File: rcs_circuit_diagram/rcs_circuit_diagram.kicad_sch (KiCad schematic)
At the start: 9 parts

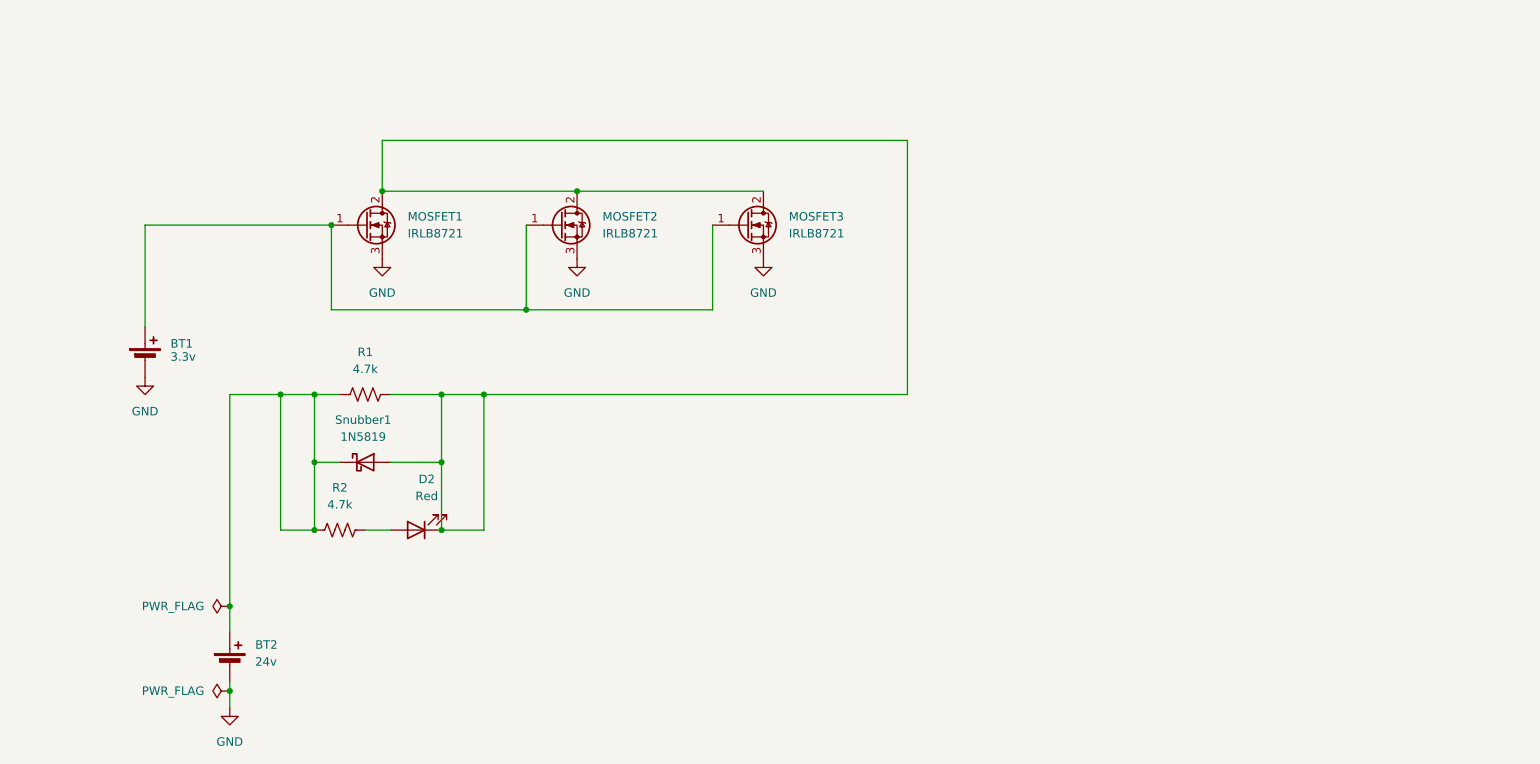
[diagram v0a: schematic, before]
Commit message: Added ext. connectors
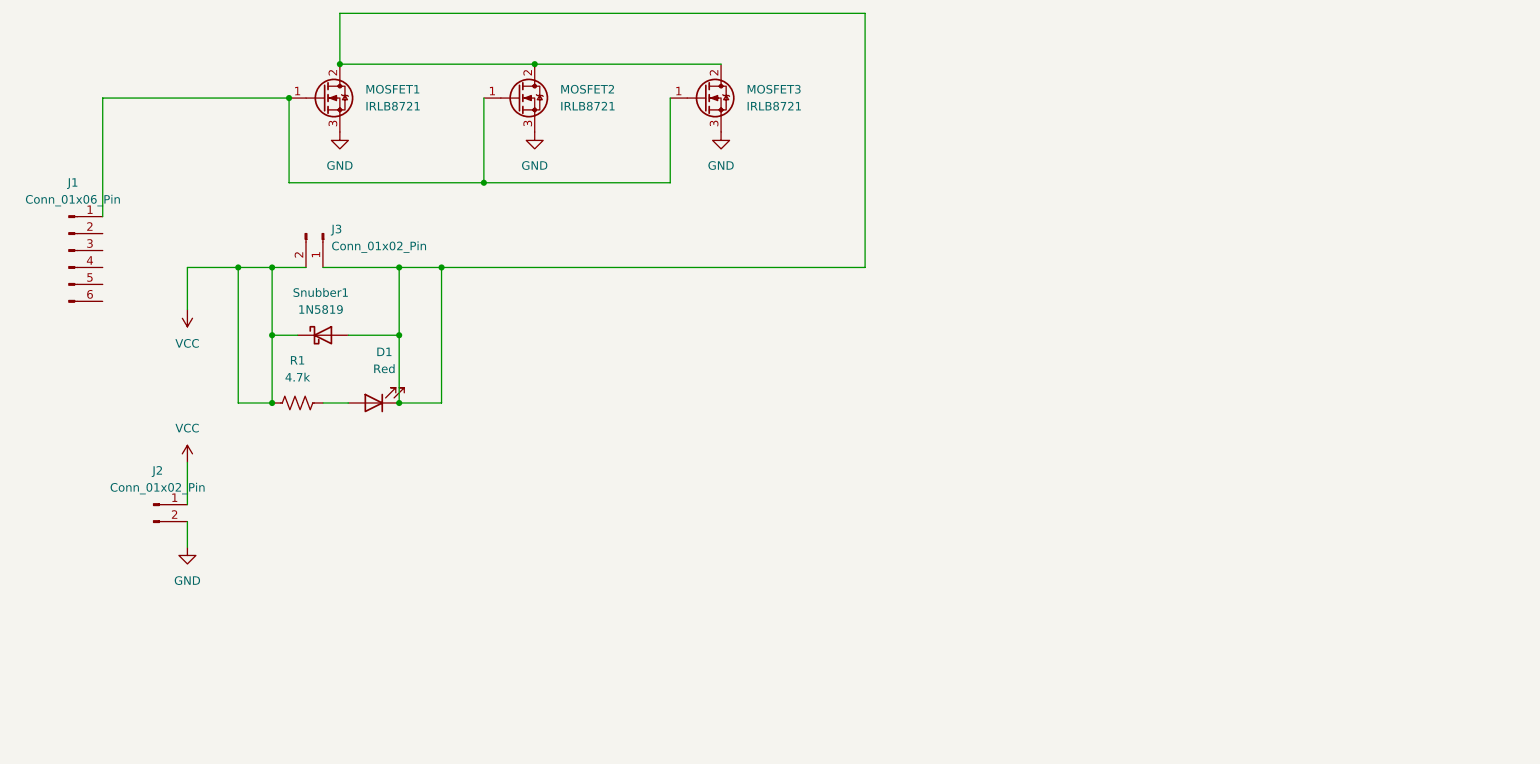
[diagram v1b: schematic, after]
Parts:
- removed BT1: 3.3v, symbol Device:Battery_Cell
- removed BT2: 24v, symbol Device:Battery_Cell
- removed D2: Red, symbol Device:LED
- removed R2: 4.7k, symbol Device:R_US
- added D1: Red, symbol Device:LED
- added J1: Conn_01x06_Pin, symbol Connector:Conn_01x06_Pin
- added J2, J3: Conn_01x02_Pin, symbol Connector:Conn_01x02_Pin
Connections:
- net GND: now also J2.2 (Pin_2)
- net VCC: now reaches R1.1, Snubber1.1 (K)
- net VCC: now also J2.1 (Pin_1), J3.2 (Pin_2)
- net at MOSFET1.2 (D), MOSFET2.2 (D), MOSFET3.2 (D)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: now also D1.1 (K), J3.1 (Pin_1); no longer R1.2
- net at MOSFET1.1 (G), MOSFET2.1 (G), MOSFET3.1 (G): now also J1.1 (Pin_1)
- new net: D1.2 (A), R1.2

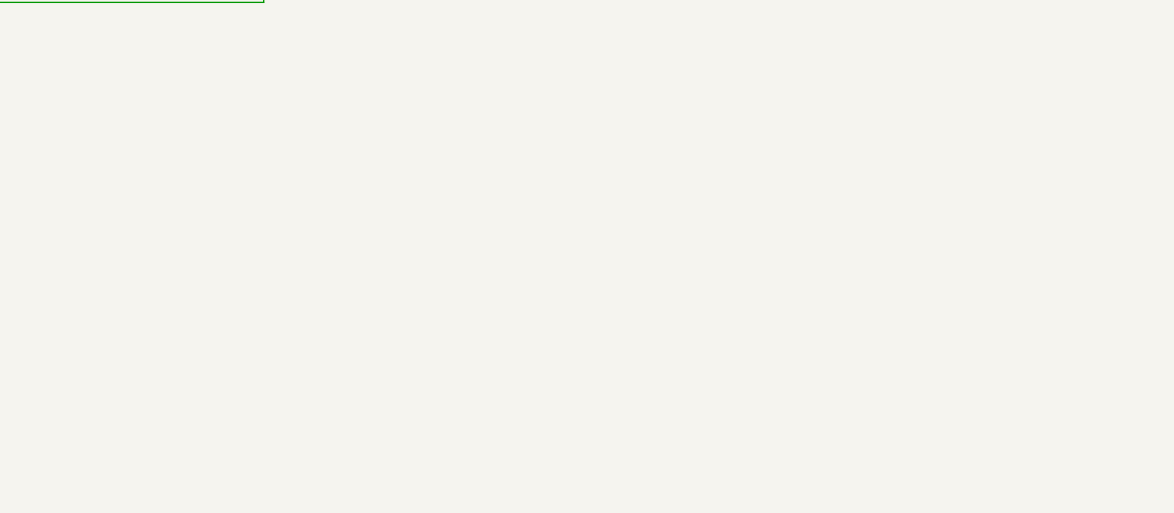
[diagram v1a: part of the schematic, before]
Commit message: Added voltage converter
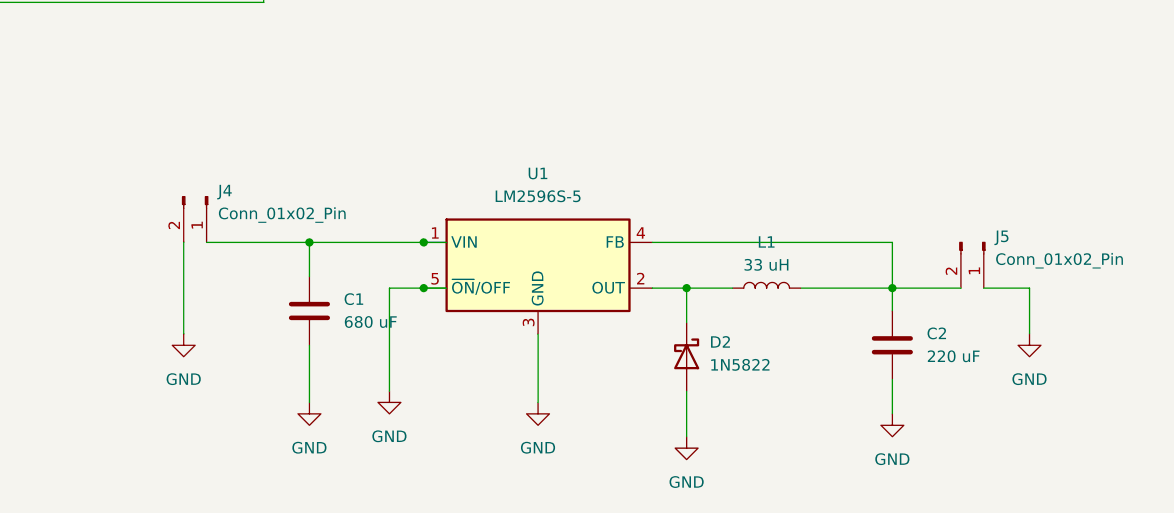
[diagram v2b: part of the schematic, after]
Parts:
- added C1: 680 uF, symbol Device:C
- added C2: 220 uF, symbol Device:C
- added D2: 1N5822, Diode_THT:D_DO-201AD_P15.24mm_Horizontal, symbol Diode:1N5822
- added J4, J5: Conn_01x02_Pin, symbol Connector:Conn_01x02_Pin
- added L1: 33 uH, symbol Device:L
- added U1: LM2596S-5, Package_TO_SOT_SMD:TO-263-5_TabPin3, symbol Regulator_Switching:LM2596S-5
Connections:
- net GND: now also C1.2, C2.2, D2.2 (A), J4.2 (Pin_2), J5.1 (Pin_1), U1.3 (GND), U1.5 (~{ON}/OFF)
- new net: C1.1, J4.1 (Pin_1), U1.1 (VIN)
- new net: D2.1 (K), L1.1, U1.2 (OUT)
- new net: C2.1, J5.2 (Pin_2), L1.2, U1.4 (FB)
